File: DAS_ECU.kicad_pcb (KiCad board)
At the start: 2 copper layers, 156.5 x 85 mm, 116 parts, among them J1 Raspberry_Pi_2_3, J10 WHEEL_RIGHT, J11 BUZZER, J2 CAN, J3 POWER, J4 SWDEBUG_CONN, J5 BRAKELIGHT, J6 PEDAL_BOX, J7 BRAKE_REAR, J8 STEERING_WHEEL, J9 WHEEL_LEFT, Q1 2N7002NXAKR, Q2 2N7002NXAKR, Q3 2N7002NXAKR, Q4 2N7002NXAKR, U1 Tex_DCDC, U10 MCP2562-E-SN, U11 MCP2562-E-SN, U12 STM32F446RETx, U13 M95256-WMN6P, U2 LD1117S50TR_SOT223, U3 MAX490E, U4 LM358, U6 LM358, U7 MCP2562-E-SN, U8 UA9637A, U9 UA9637A, Y1 ECS-160-18-33 16Mhz

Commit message: more progrees on board
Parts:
- removed RN7, RN8: 33, Resistor_SMD:R_Array_Convex_4x0603
- NT1: moved to B.Cu
- U3: footprint Package_SO:SO-8_5.3x6.2mm_P1.27mm -> Package_SO:SOIC-8_3.9x4.9mm_P1.27mm
- moved R13 90.1 mm to (174.8, 108.7), turned to 90 degrees
- moved R12 89.5 mm to (178.9, 108.7), turned to 90 degrees
- moved C11 89.3 mm to (177.4, 108.7), turned to 270 degrees
- moved RN9 88.7 mm to (189.1, 105.5), turned to 270 degrees
- moved C13 87.2 mm to (173.3, 108.7), turned to 270 degrees
- moved C16 84.0 mm to (179.6, 100.5), turned to 270 degrees
- moved RN11 79.9 mm to (189.1, 102.3), turned to 270 degrees
- moved C23 79.7 mm to (201.4, 75.2), turned to 90 degrees
- moved C21 76.0 mm to (199.7, 75.2), turned to 90 degrees
- moved FB1 75.2 mm to (197.9, 75.2), turned to 270 degrees
- moved RN6 61.0 mm to (211.2, 72.3)
- moved RN10 56.9 mm to (218.4, 108.7), turned to 270 degrees
- moved C5 55.6 mm to (220.3, 70.9), turned to 90 degrees
- moved D2 54.9 mm to (218.6, 72.7), turned to 90 degrees
- moved C6 54.8 mm to (226.1, 80.8)
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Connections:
- D2 pad 1: /Pedals_SET/ACC_1_BUF -> /Pedals_SET/ACC_2_BUF
- D3 pad 1: /Pedals_SET/ACC_2_BUF -> /Pedals_SET/ACC_1_BUF
- D4 pad 1: /Pedals_SET/BRAKE_F_BUF -> /Pedals_SET/BRAKE_R_BUF
- D5 pad 1: /Pedals_SET/BRAKE_R_BUF -> /Pedals_SET/BRAKE_F_BUF
- R10 pad 1: /Pedals_SET/BRAKE_R_BUF -> /Pedals_SET/BRAKE_F_BUF
- R3 pad 2: /Pedals_SET/ACC_S1 -> /Pedals_SET/ACC_S2
- R4 pad 2: /Pedals_SET/ACC_S2 -> /Pedals_SET/ACC_S1
- R5 pad 1: /Pedals_SET/ACC_1_BUF -> /Pedals_SET/ACC_2_BUF
- R6 pad 1: /Pedals_SET/ACC_2_BUF -> /Pedals_SET/ACC_1_BUF
- R7 pad 2: /Pedals_SET/BRAKE_SF -> /Pedals_SET/BRAKE_SR
- R8 pad 2: /Pedals_SET/BRAKE_SR -> /Pedals_SET/BRAKE_SF
- R9 pad 1: /Pedals_SET/BRAKE_F_BUF -> /Pedals_SET/BRAKE_R_BUF
- RN10 pad 1: /Brain_Rasp/WR_B -> /Brain_Rasp/WR_A
- RN10 pad 2: /Brain_Rasp/WR_A -> /Brain_Rasp/WR_B
- RN10 pad 3: /Brain_Rasp/SW_CLK -> /Brain_Rasp/SW_DATA
- RN10 pad 4: /Brain_Rasp/SW_DATA -> /Brain_Rasp/SW_CLK
- RN10 pad 5: /Encoders/SW_DATA_5 -> /Encoders/SW_CLK_5
- RN10 pad 6: /Encoders/SW_CLK_5 -> /Encoders/SW_DATA_5
- RN10 pad 7: /Encoders/WR_A_5 -> /Encoders/WR_B_5
- RN10 pad 8: /Encoders/WR_B_5 -> /Encoders/WR_A_5
- RN11 pad 7: /Brain_Rasp/WL_A -> /Brain_Rasp/WL_B
- RN11 pad 8: /Brain_Rasp/WL_B -> /Brain_Rasp/WL_A
- RN12 pad 5: /Brain_Rasp/SW_DATA -> /Brain_Rasp/SW_CLK
- RN12 pad 6: /Brain_Rasp/SW_CLK -> /Brain_Rasp/SW_DATA
- RN12 pad 7: /Brain_Rasp/WR_A -> /Brain_Rasp/WR_B
- RN12 pad 8: /Brain_Rasp/WR_B -> /Brain_Rasp/WR_A
- RN4 pad 2: Net-(RN4-Pad2) -> /~RST~
- RN4 pad 7: Net-(RN4-Pad7) -> +3V3
- RN5 pad 1: /Brain_Rasp/BRAKE_PRESSURE_FRONT -> /Brain_Rasp/ACCS_CH1
- RN5 pad 2: /Pedals_SET/BRAKE_F -> /Brain_Rasp/ACCS_CH2
- RN5 pad 3: /Brain_Rasp/ACCS_CH2 -> /Pedals_SET/BRAKE_F
- RN5 pad 4: /Brain_Rasp/ACCS_CH1 -> /Brain_Rasp/BRAKE_PRESSURE_FRONT
- RN5 pad 5: /Pedals_SET/ACC_1_BUF -> /Pedals_SET/BRAKE_R_BUF
- RN5 pad 6: /Pedals_SET/ACC_2_BUF -> /Pedals_SET/BRAKE_F_BUF
- RN5 pad 7: /Pedals_SET/BRAKE_F_BUF -> /Pedals_SET/ACC_2_BUF
- RN5 pad 8: /Pedals_SET/BRAKE_R_BUF -> /Pedals_SET/ACC_1_BUF
- RN6 pad 5: /Brain_Rasp/ACCS_CH1 -> /Brain_Rasp/BRAKE_PRESSURE_FRONT
- RN6 pad 6: /Brain_Rasp/ACCS_CH2 -> /Pedals_SET/BRAKE_F
- RN6 pad 7: /Pedals_SET/BRAKE_F -> /Brain_Rasp/ACCS_CH2
- RN6 pad 8: /Brain_Rasp/BRAKE_PRESSURE_FRONT -> /Brain_Rasp/ACCS_CH1
- RN9 pad 1: /Brain_Rasp/WL_B -> /Brain_Rasp/WL_A
- RN9 pad 2: /Brain_Rasp/WL_A -> /Brain_Rasp/WL_B
- RN9 pad 7: /Encoders/WL_A_5 -> /Encoders/WL_B_5
- RN9 pad 8: /Encoders/WL_B_5 -> /Encoders/WL_A_5
- U12 pad 10: /Brain_Rasp/ACCS_CH1 -> /Brain_Rasp/ACCS_CH2
- U12 pad 11: /Brain_Rasp/ACCS_CH2 -> /Brain_Rasp/ACCS_CH1
- U3 pad 2: Net-(RN8-Pad7) -> /Encoders/SW_DATA_5
- U3 pad 3: Net-(RN8-Pad8) -> /Encoders/SW_CLK_5
- U4 pad 1: /Pedals_SET/ACC_1_BUF -> /Pedals_SET/ACC_2_BUF
- U4 pad 7: /Pedals_SET/ACC_2_BUF -> /Pedals_SET/ACC_1_BUF
- U6 pad 1: /Pedals_SET/BRAKE_F_BUF -> /Pedals_SET/BRAKE_R_BUF
- U6 pad 7: /Pedals_SET/BRAKE_R_BUF -> /Pedals_SET/BRAKE_F_BUF
- U8 pad 2: Net-(RN7-Pad8) -> /Encoders/WL_A_5
- U8 pad 3: Net-(RN7-Pad7) -> /Encoders/WL_B_5
- U9 pad 2: Net-(RN7-Pad6) -> /Encoders/WR_A_5
- U9 pad 3: Net-(RN7-Pad5) -> /Encoders/WR_B_5
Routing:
- net +12V: track 72.0 -> 228.5 mm, vias 0 -> 4
- net GND1: track 0.00 -> 70.1 mm, vias 0 -> 18
- net /Pedals_SET/5V_SENSORS: track 0.00 -> 56.0 mm
- net +3V3: track 63.1 -> 115.4 mm
- net /Encoders/WL_B+: track 0.00 -> 48.9 mm
- net GND: track 91.7 -> 139.9 mm, vias 4 -> 12
- net /Encoders/WL_B-: track 0.00 -> 45.7 mm
- net +5V: track 146.3 -> 190.0 mm, vias 0 -> 2
- net /Encoders/WL_A+: track 0.00 -> 43.2 mm
- net /Encoders/WL_A-: track 0.00 -> 42.5 mm
- net /Encoders/WR_B-: track 0.00 -> 24.0 mm
- net /Encoders/WR_B+: track 0.00 -> 23.0 mm
- net /Encoders/WR_A-: track 0.00 -> 17.0 mm
- net /Encoders/SW_CLK+: track 0.00 -> 16.7 mm
- net /Pedals_SET/BRAKE_F: track 0.00 -> 16.1 mm
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- added copper zone on B.Cu, net GND1
- added copper zone on F.Cu, net GND1

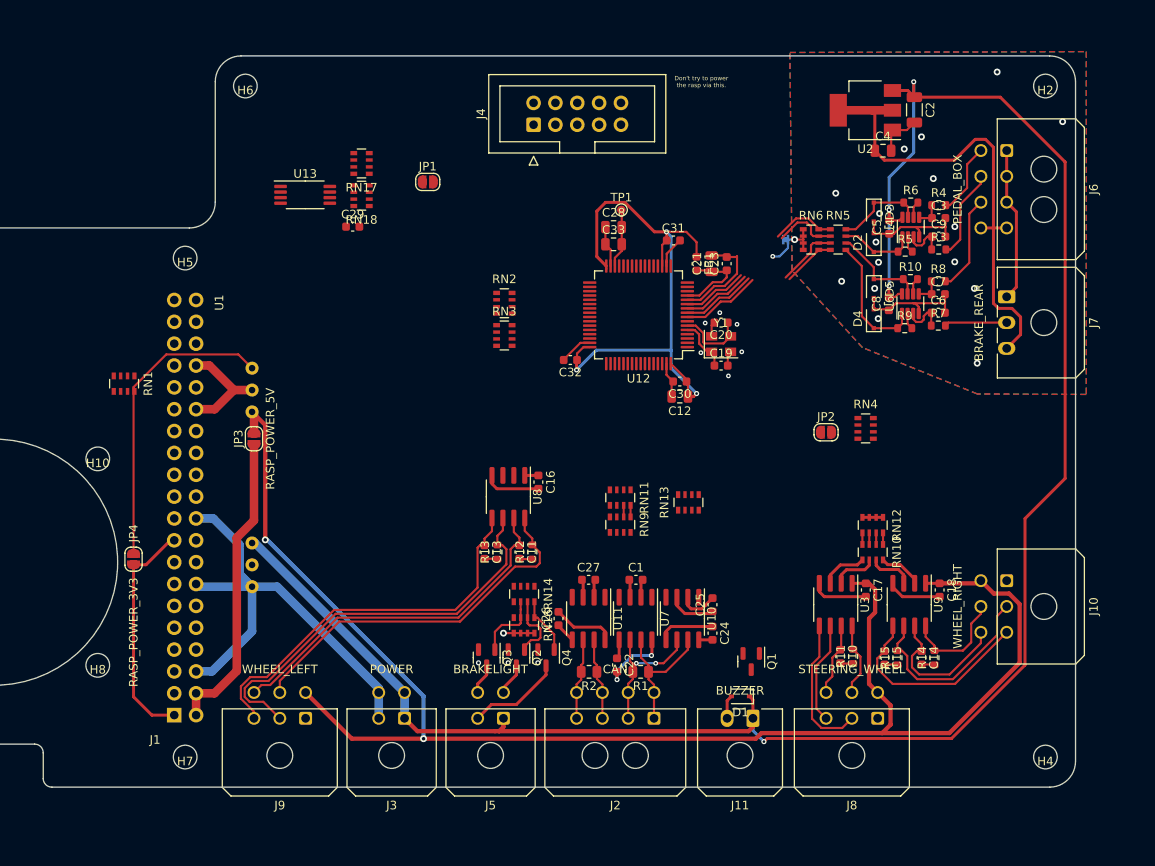
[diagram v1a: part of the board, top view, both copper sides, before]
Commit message: added IMU, pressure sensor, progress on board
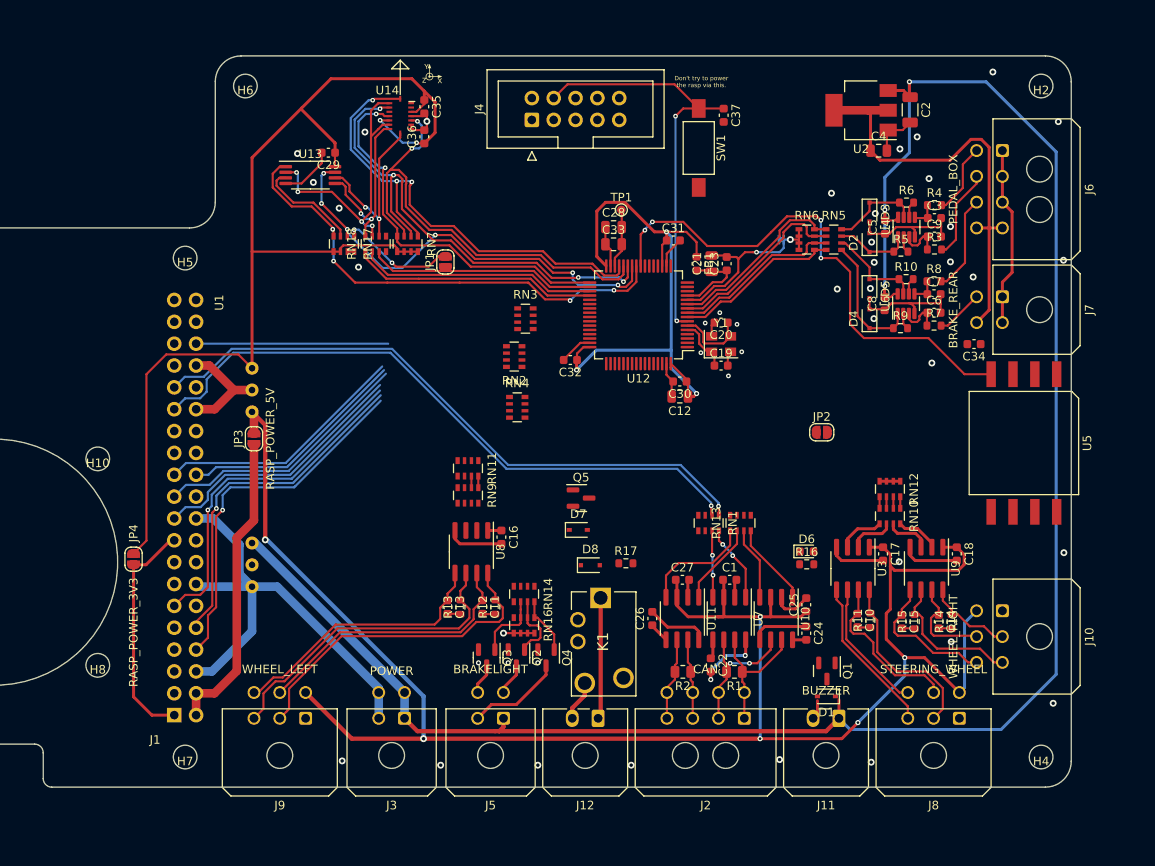
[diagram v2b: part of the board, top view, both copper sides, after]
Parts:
- added C34: 100nF, Capacitor_SMD:C_0603_1608Metric, F.Cu at (230.2, 84.5)
- added C35: 100nF, Capacitor_SMD:C_0603_1608Metric, F.Cu at (166.3, 56.9)
- added C36: 100nF, Capacitor_SMD:C_0603_1608Metric, F.Cu at (166.3, 60.4)
- added C37: 100nF, Capacitor_SMD:C_0603_1608Metric, F.Cu at (201.1, 57.9)
- added D6: LED, LED_SMD:LED_0603_1608Metric, F.Cu at (210.8, 108.6)
- added D7: 1N4148W, Diode_SMD:D_SOD-323, F.Cu at (184.2, 106.1)
- added D8: DDZ3V3ASF 3V3, Diode_SMD:D_SOD-323F, F.Cu at (185.6, 110.2)
- added G***: LOGO, Eagle_Logos:XYZ_orientation, F.Cu at (166.9, 53.4)
- added J12: SD, Connector_Molex:Molex_Micro-Fit_3.0_43650-0200_1x02_P3.00mm_Horizontal, F.Cu at (186.5, 128.0)
- added K1: EX12U1S, Eagle_Main:EX12U1S, F.Cu at (186.8, 114.0)
- added Q5: 2N7002NXAKR, Package_TO_SOT_SMD:SOT-23, F.Cu at (184.5, 102.4)
- added R16: 1k, Resistor_SMD:R_0603_1608Metric, F.Cu at (210.8, 110.1)
- added R17: 1M, Resistor_SMD:R_0603_1608Metric, F.Cu at (189.7, 110.0)
- added RN7: 100k, Resistor_SMD:R_Array_Convex_4x0603, F.Cu at (164.3, 72.8)
- added SW1: RESET, Button_Switch_SMD:SW_SPST_FSMSM, F.Cu at (198.2, 61.7)
- added U14: BMI088, Eagle_Main:Bosch_LGA-16_3x4.5mm_P0.5mm, F.Cu at (163.5, 58.0)
- added U5: MP3V5004DP, Eagle_Main:NXP_CASE_1351-01, F.Cu at (236.0, 96.0)
- J7: footprint Connector_Molex:Molex_Micro-Fit_3.0_43650-0300_1x03_P3.00mm_Horizontal -> Connector_Molex:Molex_Micro-Fit_3.0_43045-0400_2x02_P3.00mm_Horizontal
- moved RN1 69.9 mm to (199.3, 105.3)
- moved RN4 40.6 mm to (177.1, 91.8)
- moved RN11 18.0 mm to (171.4, 98.9)
- moved RN9 18.0 mm to (171.4, 102.1)
- moved C1 10.9 mm to (201.8, 111.9)
- moved C22 10.9 mm to (199.6, 121.8)
- moved C26 10.9 mm to (192.8, 116.4)
- moved C27 10.9 mm to (196.3, 111.9)
- moved R1 10.9 mm to (202.3, 122.6)
- moved R2 10.9 mm to (196.3, 122.6)
- moved U11 10.9 mm to (196.3, 116.4)
- moved U7 10.9 mm to (201.8, 116.4)
- moved C24 10.9 mm to (210.7, 118.1)
- moved C25 10.9 mm to (210.7, 114.8)
- moved U10 10.9 mm to (207.2, 116.4)
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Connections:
- net /Brain_Rasp/SPI2_MISO_1 renamed /IMU/MISO
- net /Brain_Rasp/SPI2_MOSI_1 renamed /IMU/MOSI
- net /Brain_Rasp/SPI2_SCK_1 renamed /IMU/SCK
- net /Pedals_SET/ACC_1_BUF renamed /Analog_Sensors/ACC_1_BUF
- net /Pedals_SET/ACC_2_BUF renamed /Analog_Sensors/ACC_2_BUF
- net /Pedals_SET/ACC_S1 renamed /Analog_Sensors/ACC_S1
- net /Pedals_SET/ACC_S2 renamed /Analog_Sensors/ACC_S2
- net /Pedals_SET/BRAKE_F renamed /Analog_Sensors/BRAKE_F
- net /Pedals_SET/BRAKE_F_BUF renamed /Analog_Sensors/BRAKE_F_BUF
- net /Pedals_SET/BRAKE_R_BUF renamed /Analog_Sensors/BRAKE_R_BUF
- net /Pedals_SET/BRAKE_SF renamed /Analog_Sensors/BRAKE_SF
- C4 pad 1: /Pedals_SET/5V_SENSORS -> /Analog_Sensors/5V_SENSORS
- J10 pad 2: /Encoders/WR_B+ -> /Encoders/WR_A+
- J10 pad 3: /Encoders/WR_B- -> /Encoders/WR_B+
- J10 pad 5: /Encoders/WR_A+ -> /Encoders/WR_A-
- J10 pad 6: /Encoders/WR_A- -> /Encoders/WR_B-
- J6 pad 4: /Pedals_SET/5V_SENSORS -> /Analog_Sensors/5V_SENSORS
- J6 pad 8: /Pedals_SET/5V_SENSORS -> /Analog_Sensors/5V_SENSORS
- J7 pad 2: /Pedals_SET/BRAKE_SR -> GND1
- J7 pad 3: /Pedals_SET/5V_SENSORS -> /Analog_Sensors/BRAKE_SR
- J8 pad 2: /Encoders/SW_CLK+ -> /Encoders/SW_DATA+
- J8 pad 3: /Encoders/SW_CLK- -> /Encoders/SW_CLK+
- J8 pad 5: /Encoders/SW_DATA+ -> /Encoders/SW_DATA-
- J8 pad 6: /Encoders/SW_DATA- -> /Encoders/SW_CLK-
- J9 pad 2: /Encoders/WL_B+ -> /Encoders/WL_A+
- J9 pad 3: /Encoders/WL_B- -> /Encoders/WL_B+
- J9 pad 5: /Encoders/WL_A+ -> /Encoders/WL_A-
- J9 pad 6: /Encoders/WL_A- -> /Encoders/WL_B-
- R7 pad 2: /Pedals_SET/BRAKE_SR -> /Analog_Sensors/BRAKE_SR
- RN1 pad 1: Net-(RN1-Pad1) -> /Brain_Rasp/CANTX_NVIDIA
- RN1 pad 2: Net-(RN1-Pad2) -> /Brain_Rasp/CANRX_NVIDIA
- RN1 pad 7: /Brain_Rasp/CANRX_NVIDIA -> Net-(RN1-Pad7)
- RN1 pad 8: /Brain_Rasp/CANTX_NVIDIA -> Net-(RN1-Pad8)
- RN13 pad 4: /Brain_Rasp/CAN2_RX -> Net-(RN13-Pad4)
- RN13 pad 5: Net-(RN13-Pad5) -> /Brain_Rasp/CAN1_TX
- RN13 pad 6: /Brain_Rasp/CAN2_TX -> /Brain_Rasp/CAN1_RX
- RN13 pad 7: /Brain_Rasp/CAN1_RX -> /Brain_Rasp/CAN2_TX
- RN13 pad 8: /Brain_Rasp/CAN1_TX -> /Brain_Rasp/CAN2_RX
- RN14 pad 4: Net-(RN14-Pad4) -> /SD_CLOSE
- RN14 pad 5: Net-(RN14-Pad5) -> /SD_CLOSE_G
- RN16 pad 4: Net-(RN16-Pad4) -> /SD_CLOSE_G
- RN17 pad 1: GND -> Net-(JP1-Pad2)
- RN17 pad 2: GND -> /Brain_Rasp/~HOLD~
- RN17 pad 3: +3V3 -> /Brain_Rasp/~W~
- RN17 pad 4: +3V3 -> /Brain_Rasp/~CS_EEPROM~
- RN17 pad 5: /Brain_Rasp/~CS_EEPROM~ -> +3V3
- RN17 pad 6: /Brain_Rasp/~W~ -> +3V3
- RN17 pad 7: /Brain_Rasp/~HOLD~ -> GND
- RN17 pad 8: Net-(JP1-Pad2) -> GND
- RN2 pad 1: /Brain_Rasp/RASP_CTS -> /Brain_Rasp/MCU_RTS
- RN2 pad 2: /Brain_Rasp/RASP_RTS -> /Brain_Rasp/MCU_CTS
- RN2 pad 3: /Brain_Rasp/RASP_TX -> /Brain_Rasp/MCU_RX
- RN2 pad 4: /Brain_Rasp/RASP_RX -> /Brain_Rasp/MCU_TX
- RN2 pad 5: /Brain_Rasp/MCU_TX -> /Brain_Rasp/RASP_RX
- RN2 pad 6: /Brain_Rasp/MCU_RX -> /Brain_Rasp/RASP_TX
- RN2 pad 7: /Brain_Rasp/MCU_CTS -> /Brain_Rasp/RASP_RTS
- RN2 pad 8: /Brain_Rasp/MCU_RTS -> /Brain_Rasp/RASP_CTS
- RN4 pad 2: /~RST~ -> /Brain_Rasp/MCU_SPI_CS
- RN4 pad 4: /Brain_Rasp/BUZZER -> /Brain_Rasp/BUZZER_1
- U10 pad 1: Net-(RN13-Pad1) -> Net-(RN13-Pad4)
- U10 pad 4: Net-(RN13-Pad2) -> Net-(RN13-Pad3)
- U11 pad 1: Net-(RN13-Pad3) -> Net-(RN13-Pad2)
- U11 pad 4: Net-(RN13-Pad5) -> Net-(RN13-Pad1)
- U12 pad 2: Net-(U12-Pad2) -> /SD_IN_3V3
- U12 pad 24: Net-(U12-Pad24) -> /Analog_Sensors/PITOT_PD
- U12 pad 25: Net-(U12-Pad25) -> /Brain_Rasp/~CS_EEPROM~
- U12 pad 26: Net-(U12-Pad26) -> /Brain_Rasp/~HOLD~
- U12 pad 27: Net-(U12-Pad27) -> /Brain_Rasp/CSB_ACC
- U12 pad 28: Net-(U12-Pad28) -> /Brain_Rasp/CSB_GYR
- U12 pad 29: Net-(U12-Pad29) -> /Brain_Rasp/ACC_INT
- U12 pad 3: Net-(U12-Pad3) -> /MCU_GPIO
- U12 pad 33: Net-(U12-Pad33) -> /Brain_Rasp/GYR_INT
- U12 pad 4: Net-(U12-Pad4) -> /SD_CLOSE
- U12 pad 41: Net-(U12-Pad41) -> /Brain_Rasp/BUZZER
- U2 pad 2: /Pedals_SET/5V_SENSORS -> /Analog_Sensors/5V_SENSORS
- U7 pad 1: Net-(RN1-Pad1) -> Net-(RN1-Pad8)
- U7 pad 4: Net-(RN1-Pad2) -> Net-(RN1-Pad7)
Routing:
- net +3V3: track 115.4 -> 210.4 mm, vias 3 -> 5
- net /Brain_Rasp/CANRX_NVIDIA: track 0.00 -> 74.7 mm, vias 0 -> 1
- net /Brain_Rasp/CANTX_NVIDIA: track 0.00 -> 74.0 mm, vias 0 -> 1
- net /Analog_Sensors/PITOT_PD: track 0.00 -> 61.4 mm, vias 0 -> 4
- net /Brain_Rasp/CSB_ACC: track 0.00 -> 57.9 mm, vias 0 -> 4
- net /Brain_Rasp/ACC_INT: track 0.00 -> 57.9 mm, vias 0 -> 3
- net /Brain_Rasp/~CS_EEPROM~: track 0.00 -> 57.0 mm, vias 0 -> 4
- net /Pedals_SET/5V_SENSORS: track 56.0 -> 0.00 mm
- net /Brain_Rasp/CSB_GYR: track 0.00 -> 53.0 mm, vias 0 -> 2
- net /Brain_Rasp/~HOLD~: track 0.00 -> 51.8 mm, vias 0 -> 6
- net /Analog_Sensors/5V_SENSORS: track 0.00 -> 50.7 mm
- net /~RST~: track 0.00 -> 49.8 mm, vias 0 -> 2
- net /Brain_Rasp/GYR_INT: track 0.00 -> 44.8 mm, vias 0 -> 2
- net /Brain_Rasp/RASP_TX: track 0.00 -> 42.2 mm, vias 0 -> 1
- net /Brain_Rasp/RASP_RTS: track 0.00 -> 40.3 mm, vias 0 -> 1
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- removed copper zone on B.Cu, net GND1
- removed copper zone on F.Cu, net GND1
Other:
- board size 156.5 x 85 mm -> 156 x 85 mm
- net class Default: via_dia 0.8 -> 0.55; via_drill 0.4 -> 0.25
